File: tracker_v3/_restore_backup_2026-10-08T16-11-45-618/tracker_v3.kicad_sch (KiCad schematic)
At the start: 16 parts, among them J2 P70-7000045, J3 P70-7000045, U1 XIAO-ESP32-DIP, U2 LIS3DH, U4 INA226AIDGSR

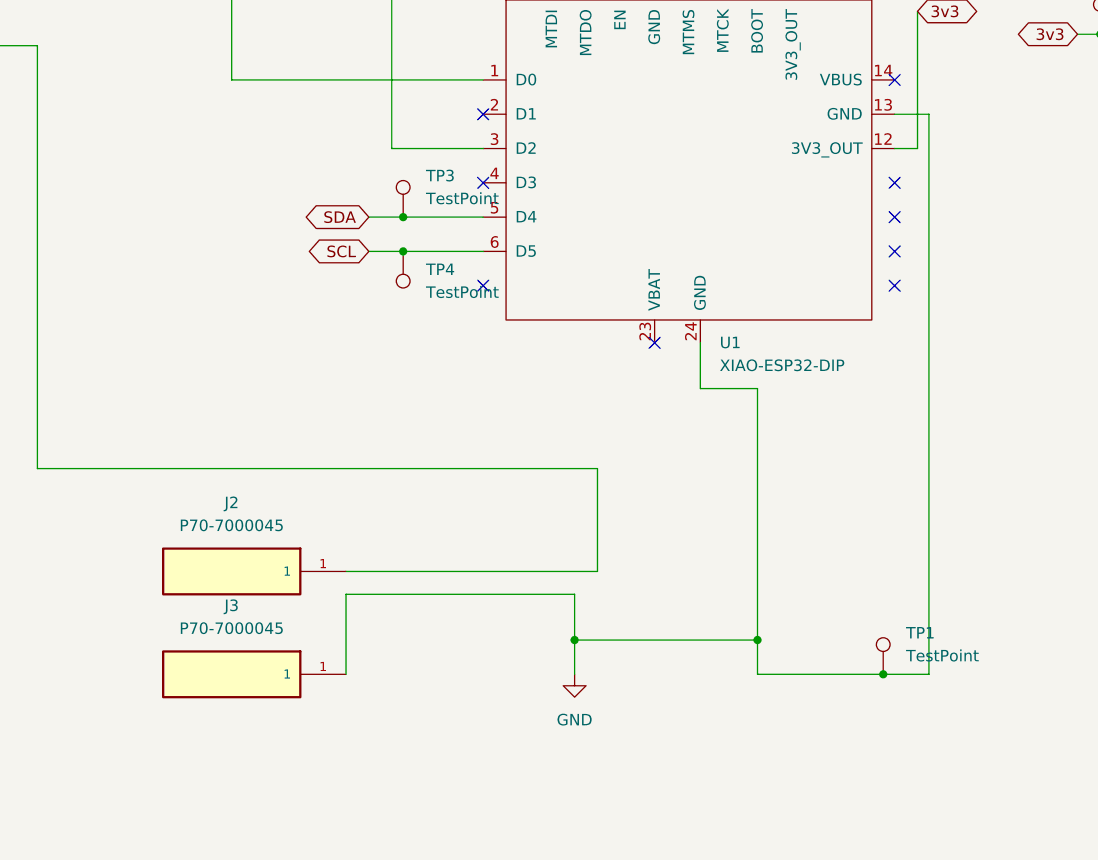
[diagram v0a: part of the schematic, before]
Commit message: added pogo pins to tracker_v3
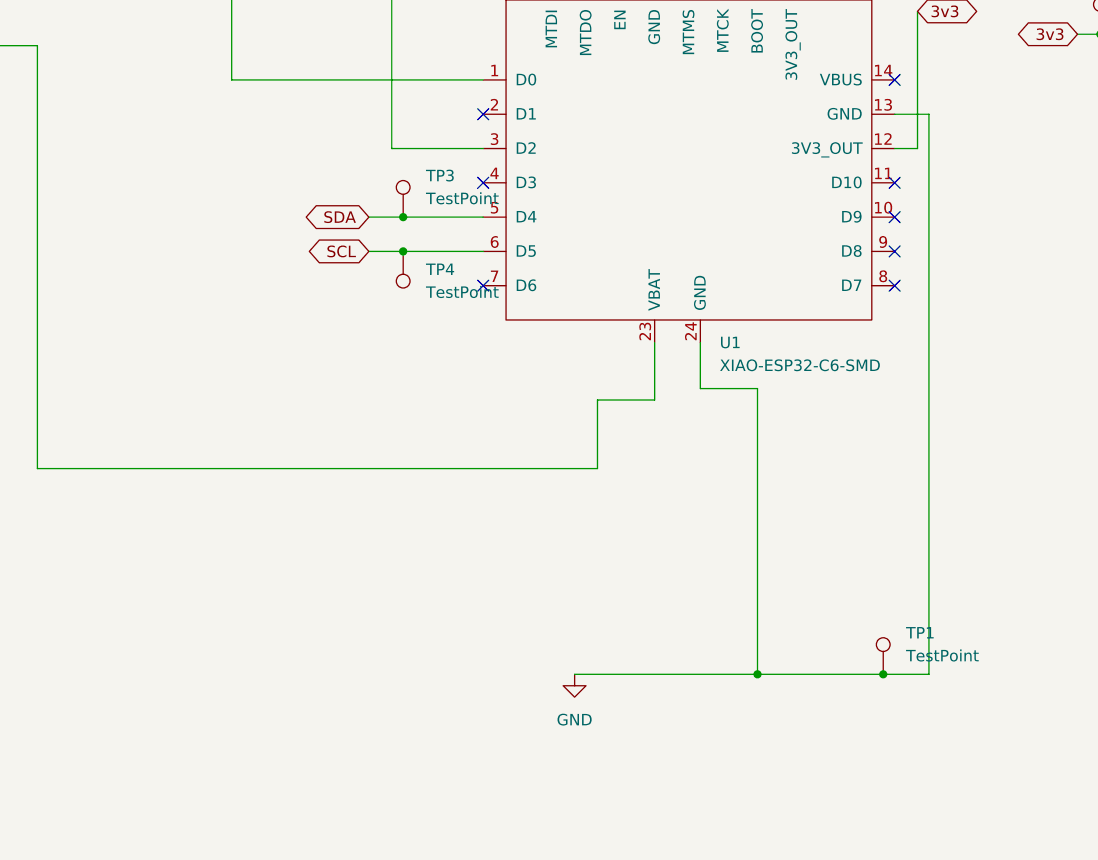
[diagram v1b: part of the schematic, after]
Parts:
- removed J2, J3: P70-7000045, P70_7000045:HARWIN_P70-7000045, symbol P70-7000045:P70-7000045
- U1: value XIAO-ESP32-DIP -> XIAO-ESP32-C6-SMD
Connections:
- net Shunt_Output: now also U1.23 (VBAT)
- no-connect marks 21 -> 20
